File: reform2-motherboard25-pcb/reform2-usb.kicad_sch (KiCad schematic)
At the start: 73 parts, among them J14 USB_INT2, J17 USB3_A, J5 USB3_A, J6 USB3_A, J9 USB_INT1, U21 SP3012-06UTG, U25 SP3012-06UTG, U26 SP3012-06UTG, U9 TUSB8040PFP, Y1 24MHz

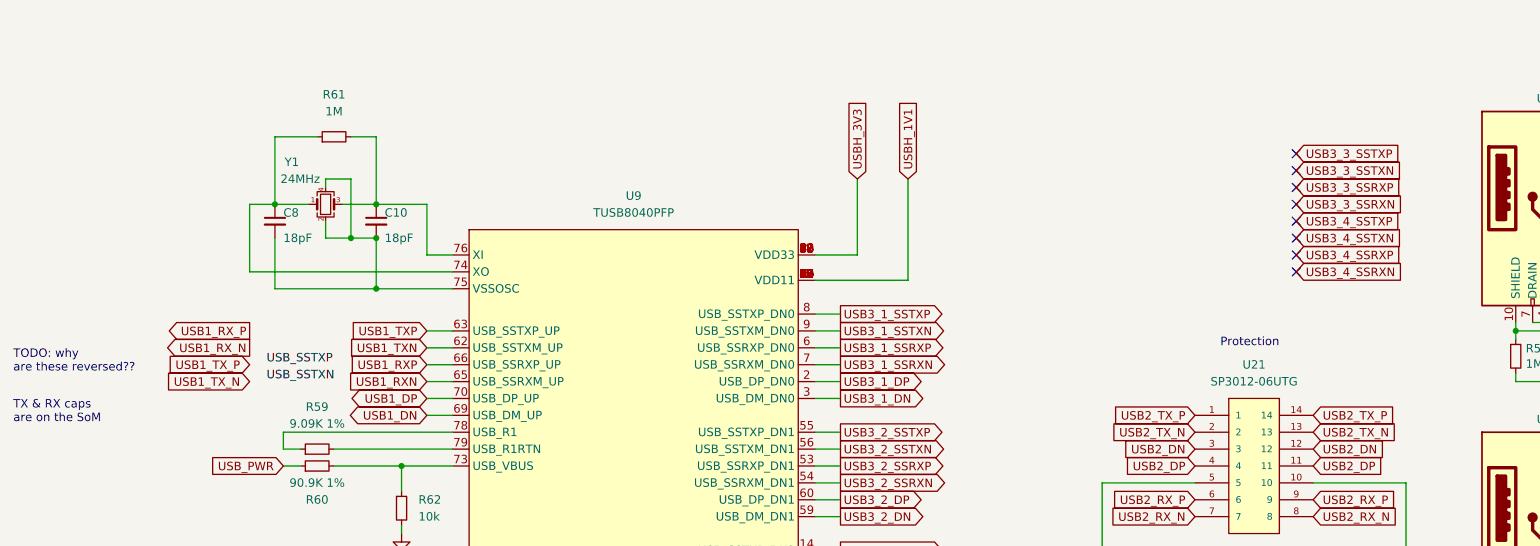
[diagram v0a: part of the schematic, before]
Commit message: mb25-pcb: routing snapshot (0 unrouted)
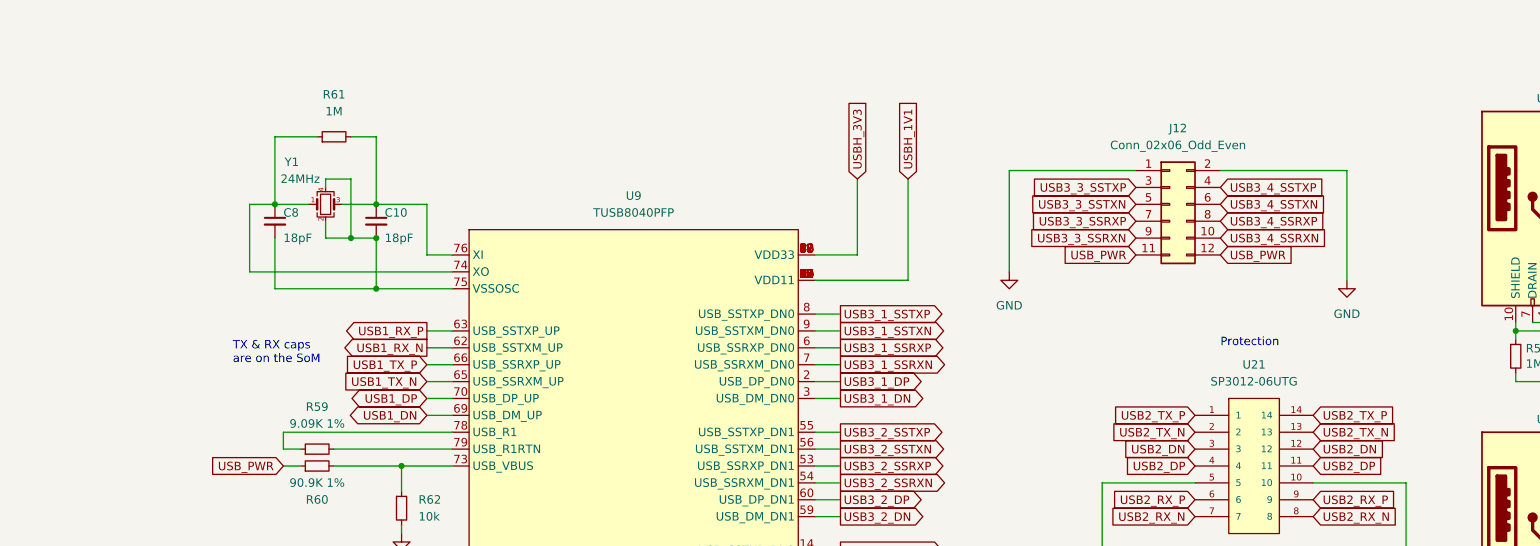
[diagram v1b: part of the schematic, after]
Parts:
- added J12: Conn_02x06_Odd_Even, Connector_PinHeader_1.00mm:PinHeader_2x06_P1.00mm_Vertical_SMD, symbol Connector_Generic:Conn_02x06_Odd_Even
- C11, C12, C13, C14, C15, C20, C21, C43, C66, C73, C86, C87, C88, C89, C9, C90, C91, C92: footprint Capacitor_SMD:C_0402_1005Metric -> Capacitor_SMD:C_0603_1608Metric
- R59, R60, R61, R62, R63, R81, R84, R85: footprint Resistor_SMD:R_0402_1005Metric -> Resistor_SMD:R_0603_1608Metric
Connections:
- net USB1_RXN is gone; now on net USB1_TX_N: U9.65 (USB_SSRXM_UP)
- net USB1_RXP is gone; now on net USB1_TX_P: U9.66 (USB_SSRXP_UP)
- net USB1_TXN is gone; now on net USB1_RX_N: U9.62 (USB_SSTXM_UP)
- net USB1_TXP is gone; now on net USB1_RX_P: U9.63 (USB_SSTXP_UP)
- net GND: now also J12.1 (Pin_1), J12.2 (Pin_2)
- net USB3_3_SSRXN: now also J12.9 (Pin_9)
- net USB3_3_SSRXP: now also J12.7 (Pin_7)
- net USB3_3_SSTXN: now also J12.5 (Pin_5)
- net USB3_3_SSTXP: now also J12.3 (Pin_3)
- net USB3_4_SSRXN: now also J12.10 (Pin_10)
- net USB3_4_SSRXP: now also J12.8 (Pin_8)
- net USB3_4_SSTXN: now also J12.6 (Pin_6)
- net USB3_4_SSTXP: now also J12.4 (Pin_4)
- net USB_PWR: now also J12.11 (Pin_11), J12.12 (Pin_12)
- no-connect marks 16 -> 8
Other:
- note removed: "TODO: why are these reversed??"

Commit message: motherboard 2.5 snapshot: fully routed and cleaned up
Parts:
- C11, C12, C13, C14, C15, C20, C21, C43, C66, C86, C88, C9, C90: LCSC C1525 -> (none); Manufacturer Samsung -> Yageo; Manufacturer_No CL05B104KO5NNNC -> CC0603JPX7R9BB104
- C39, C40, C41, C42, C67, C70, C74, C75, C76, C77, C84, C85: Distributor Mouser -> (none)
- R62, R63, R84, R85: LCSC C60490 -> (none); Manufacturer_No RC0402FR-0710KL -> RC0603FR-0710KL
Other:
- note added: "1V1 is slightly overdriven by 1.2V. Datasheet says 1.26V max."
- note removed: "TODO: does it tolerate 1.2V? (vs 1V1)"

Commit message: motherboard25: r-1 snapshot, ordered for test bringup
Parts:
- C11, C12, C13, C14, C15, C20, C21, C43, C66, C86, C88, C9, C90: Checked (none) -> y
- C73, C87, C89: Checked (none) -> y; Distributor (none) -> Mouser; LCSC C14445 -> (none); Manufacturer Samsung -> Taiyo Yuden; Manufacturer_No CL05A105KP5NNNC -> UMK107BJ105KA-T
- C91, C92: Checked (none) -> y; Distributor (none) -> Mouser; LCSC C315248 -> (none); Manufacturer Samsung -> Murata; Manufacturer_No CL05A106MP5NUNC -> GRM188R6YA106MA73D
- J12: value Conn_02x06_Odd_Even -> Conn_02x08_Odd_Even; footprint Connector_PinHeader_1.00mm:PinHeader_2x06_P1.00mm_Vertical_SMD -> Connector_PinHeader_1.00mm:PinHeader_2x08_P1.00mm_Vertical_SMD; symbol Connector_Generic:Conn_02x06_Odd_Even -> Connector_Generic:Conn_02x08_Odd_Even; Distributor (none) -> Mouser; Manufacturer (none) -> Harwin; Manufacturer_No (none) -> M40-3200845R
- R59: Checked (none) -> y; Distributor (none) -> Mouser; LCSC C400642 -> (none); Manufacturer Panasonic -> Vishay Dale; Manufacturer_No ERJ2RKF9091X -> CRCW06039K09FKTA
- R60: Checked (none) -> y; Distributor (none) -> Mouser; LCSC C26989 -> (none); Manufacturer UNI-ROYAL -> Vishay Dale; Manufacturer_No 0402WGF9092TCE -> CRCW060390K9FKEA
- R61: Checked (none) -> y; Distributor (none) -> Mouser; LCSC C144787 -> (none); Manufacturer_No AC0402FR-071ML -> RC0603FR-071ML
- R62, R63, R84, R85: Checked (none) -> y; Distributor (none) -> Mouser
- R81: LCSC C242160 -> (none); Manufacturer Panasonic -> Vishay Dale; Manufacturer_No ERJ2GE0R00X -> CRCW06030000Z0EAC
- U21, U25, U26: Field12 0.5 -> (none); Field13 0.0 -> (none); Field14 3.4 -> (none); Field15 02/23/17 -> (none); Field17 0.55 -> (none); Field18 0.25 -> (none); Field21 0.35 -> (none); Field22 0.55mm -> (none); Field23 0.2 -> (none); Field25 14.0 -> (none); Field28 0.15 -> (none); Field30 0.25 -> (none); Field33 3.6 -> (none); Field34 0.0 -> (none); Field38 IPC 7351B -> (none); Field39 1.35 -> (none); Field40 3.5 -> (none); Field42 Littelfuse -> (none); Field43 0.3 -> (none); Field5 1.45 -> (none); Field6 1.25 -> (none)
- U9: Checked (none) -> y; Distributor (none) -> TI
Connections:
- net GND: now also J12.15 (Pin_15), J12.16 (Pin_16)
- net USB_PWR: now also J12.13 (Pin_13), J12.14 (Pin_14)
